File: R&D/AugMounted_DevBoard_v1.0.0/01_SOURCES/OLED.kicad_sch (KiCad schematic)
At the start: 27 parts, among them U401 U_TXS0108E, U402 U_TXS0108E, U403 U_TXS0108E

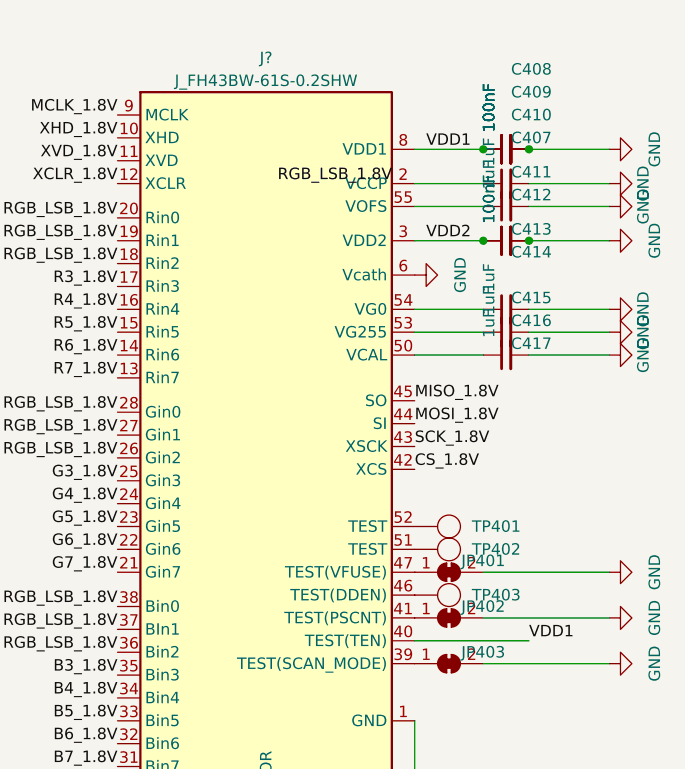
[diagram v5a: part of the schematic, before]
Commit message: Component layout is done, routing video signals is done too.
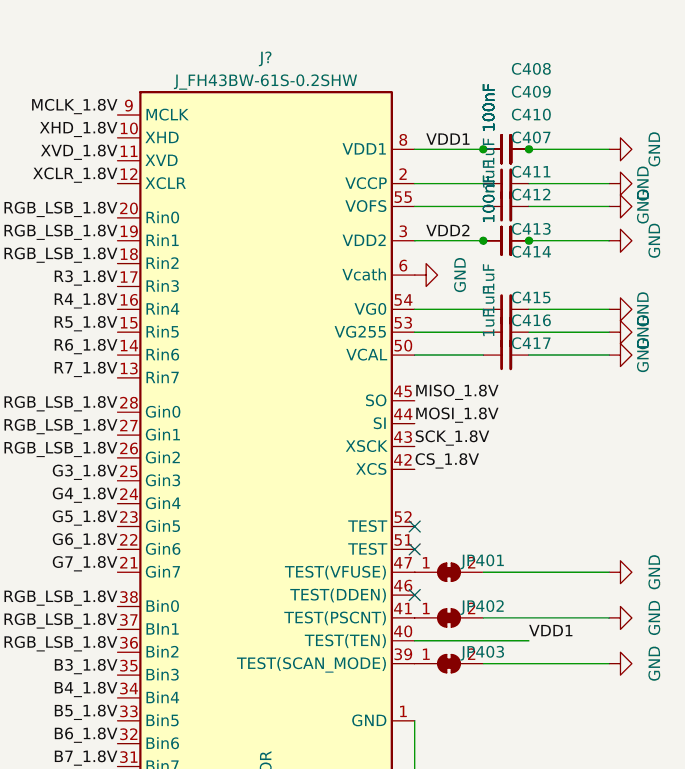
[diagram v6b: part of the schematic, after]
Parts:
- removed TP401, TP402, TP403: TESTPOINT_1MM, .mounted-lib:TESTPOINT_1MM, symbol .mounted-lib:TESTPOINT_1MM
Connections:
- no-connect marks 0 -> 3
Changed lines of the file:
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@@
   (junction (at 214.63 106.68) (diameter 0) (color 0 0 0 0)
   )
+  (no_connect (at 276.86 87.63))
+  (no_connect (at 276.86 95.25))
+  (no_connect (at 276.86 90.17))
   (wire (pts (xy 218.44 24.13) (xy 214.63 24.13))
     (stroke (width 0) (type default))
@@
     (effects (font (size 1.27 1.27)) (justify left bottom))
   )
-  (label "RGB_LSB_1.8V" (at 261.62 49.53 0) (fields_autoplaced)
-    (effects (font (size 1.27 1.27)) (justify left bottom))
-  )
   (label "B6_1.8V" (at 243.84 111.76 180) (fields_autoplaced)
     (effects (font (size 1.27 1.27)) (justify right bottom))
@@
     )
   )
-  (symbol (lib_id ".mounted-lib:TESTPOINT_1MM") (at 280.67 87.63 180) (unit 1)
-    (in_bom no) (on_board yes) (dnp no)
-    (property "Reference" "TP401" (at 283.21 87.63 0)
-      (effects (font (size 1.27 1.27)) (justify right))
-    )
-    (property "Value" "TESTPOINT_1MM" (at 261.62 87.63 0)
-      (effects (font (size 1.27 1.27)) (justify left) hide)
-    )
-    (property "Footprint" ".mounted-lib:TESTPOINT_1MM" (at 261.62 85.09 0)
-      (effects (font (size 1.27 1.27)) (justify left) hide)
-    )
-    (property "Datasheet" "http://127.0.0.1" (at 261.62 82.55 0)
-      (effects (font (size 1.27 1.27)) (justify left) hide)
-    )
-    (property "DisplayValue" "1mm" (at 283.21 88.9 0)
-      (effects (font (size 1.27 1.27)) (justify right) hide)
-    )
-    (property "_Created" "JCN 2022-08-04" (at 252.73 80.01 0)
-      (effects (font (size 1.27 1.27)) hide)
-    )
-    (property "Category" "TEST POINT" (at 261.62 74.93 0)
-      (effects (font (size 1.27 1.27)) (justify left) hide)
-    )
-    (property "Family" "Exposed copper" (at 261.62 77.47 0)
-      (effects (font (size 1.27 1.27)) (justify left) hide)
-    )
-    (pin "1")
-    (instances
-      (project "AugMounted_DevBoard"
-        (path "/75b08848-9393-425e-a17d-60105119a7b1/a5fd713b-0eff-4c6e-9443-f8836b4c4660"
-          (reference "TP401") (unit 1)
-        )
-      )
-    )
-  )
   (symbol (lib_id "Jumper:SolderJumper_2_Bridged") (at 280.67 92.71 0) (unit 1)
     (in_bom yes) (on_board yes) (dnp no)
@@
     )
   )
-  (symbol (lib_id ".mounted-lib:TESTPOINT_1MM") (at 280.67 95.25 180) (unit 1)
-    (in_bom no) (on_board yes) (dnp no)
-    (property "Reference" "TP403" (at 283.21 95.25 0)
-      (effects (font (size 1.27 1.27)) (justify right))
-    )
-    (property "Value" "TESTPOINT_1MM" (at 261.62 95.25 0)
-      (effects (font (size 1.27 1.27)) (justify left) hide)
-    )
-    (property "Footprint" ".mounted-lib:TESTPOINT_1MM" (at 261.62 92.71 0)
-      (effects (font (size 1.27 1.27)) (justify left) hide)
-    )
-    (property "Datasheet" "http://127.0.0.1" (at 261.62 90.17 0)
-      (effects (font (size 1.27 1.27)) (justify left) hide)
-    )
-    (property "DisplayValue" "1mm" (at 283.21 96.52 0)
-      (effects (font (size 1.27 1.27)) (justify right) hide)
-    )
-    (property "_Created" "JCN 2022-08-04" (at 252.73 87.63 0)
-      (effects (font (size 1.27 1.27)) hide)
-    )
-    (property "Category" "TEST POINT" (at 261.62 82.55 0)
-      (effects (font (size 1.27 1.27)) (justify left) hide)
-    )
-    (property "Family" "Exposed copper" (at 261.62 85.09 0)
-      (effects (font (size 1.27 1.27)) (justify left) hide)
-    )
-    (pin "1")
-    (instances
-      (project "AugMounted_DevBoard"
-        (path "/75b08848-9393-425e-a17d-60105119a7b1/a5fd713b-0eff-4c6e-9443-f8836b4c4660"
-          (reference "TP403") (unit 1)
-        )
-      )
-    )
-  )
   (symbol (lib_id ".mounted-lib:C_0402_100nF_50V_X7R_10%") (at 214.63 29.21 0) (unit 1)
     (in_bom yes) (on_board yes) (dnp no) (fields_autoplaced)
@@
         )
       )
-    )
-  )
-  (symbol (lib_id ".mounted-lib:TESTPOINT_1MM") (at 280.67 90.17 180) (unit 1)
-    (in_bom no) (on_board yes) (dnp no)
-    (property "Reference" "TP402" (at 283.21 90.17 0)
-      (effects (font (size 1.27 1.27)) (justify right))
-    )
-    (property "Value" "TESTPOINT_1MM" (at 261.62 90.17 0)
-      (effects (font (size 1.27 1.27)) (justify left) hide)
-    )
-    (property "Footprint" ".mounted-lib:TESTPOINT_1MM" (at 261.62 87.63 0)
-      (effects (font (size 1.27 1.27)) (justify left) hide)
-    )
-    (property "Datasheet" "http://127.0.0.1" (at 261.62 85.09 0)
-      (effects (font (size 1.27 1.27)) (justify left) hide)
-    )
-    (property "DisplayValue" "1mm" (at 283.21 91.44 0)
-      (effects (font (size 1.27 1.27)) (justify right) hide)
-    )
-    (property "_Created" "JCN 2022-08-04" (at 252.73 82.55 0)
-      (effects (font (size 1.27 1.27)) hide)
-    )
-    (property "Category" "TEST POINT" (at 261.62 77.47 0)
-      (effects (font (size 1.27 1.27)) (justify left) hide)
-    )
-    (property "Family" "Exposed copper" (at 261.62 80.01 0)
-      (effects (font (size 1.27 1.27)) (justify left) hide)
-    )
-    (pin "1")
-    (instances
-      (project "AugMounted_DevBoard"
-        (path "/75b08848-9393-425e-a17d-60105119a7b1/a5fd713b-0eff-4c6e-9443-f8836b4c4660"
-          (reference "TP402") (unit 1)
-        )
-      )

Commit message: Layout almost done
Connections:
- net 1.8V is gone; now on net +1V8: U401.10 (OE), U402.10 (OE), U403.10 (OE)
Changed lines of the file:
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@@
+    (effects (font (size 1.27 1.27)) (justify left bottom))
+  )
+  (label "1.8V" (at 199.39 24.13 0) (fields_autoplaced)
     (effects (font (size 1.27 1.27)) (justify left bottom))
   )
@@
   )
   (label "G7_1.8V" (at 199.39 73.66 0) (fields_autoplaced)
+    (effects (font (size 1.27 1.27)) (justify left bottom))
+  )
+  (label "1.8V" (at 204.47 106.68 0) (fields_autoplaced)
     (effects (font (size 1.27 1.27)) (justify left bottom))
   )
@@
     (effects (font (size 1.27 1.27)) (justify right bottom))
   )
+  (label "1.8V" (at 199.39 64.77 0) (fields_autoplaced)
+    (effects (font (size 1.27 1.27)) (justify left bottom))
+  )
   (label "RGB_LSB_1.8V" (at 243.84 80.01 180) (fields_autoplaced)
